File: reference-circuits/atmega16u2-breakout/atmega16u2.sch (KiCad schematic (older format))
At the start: 24 parts, among them J1 USB-MICROB, J2 ICSP, U1 IC-MCU-ATMEGA16U2-MU-VQFN32, X1 16MHz 18pF

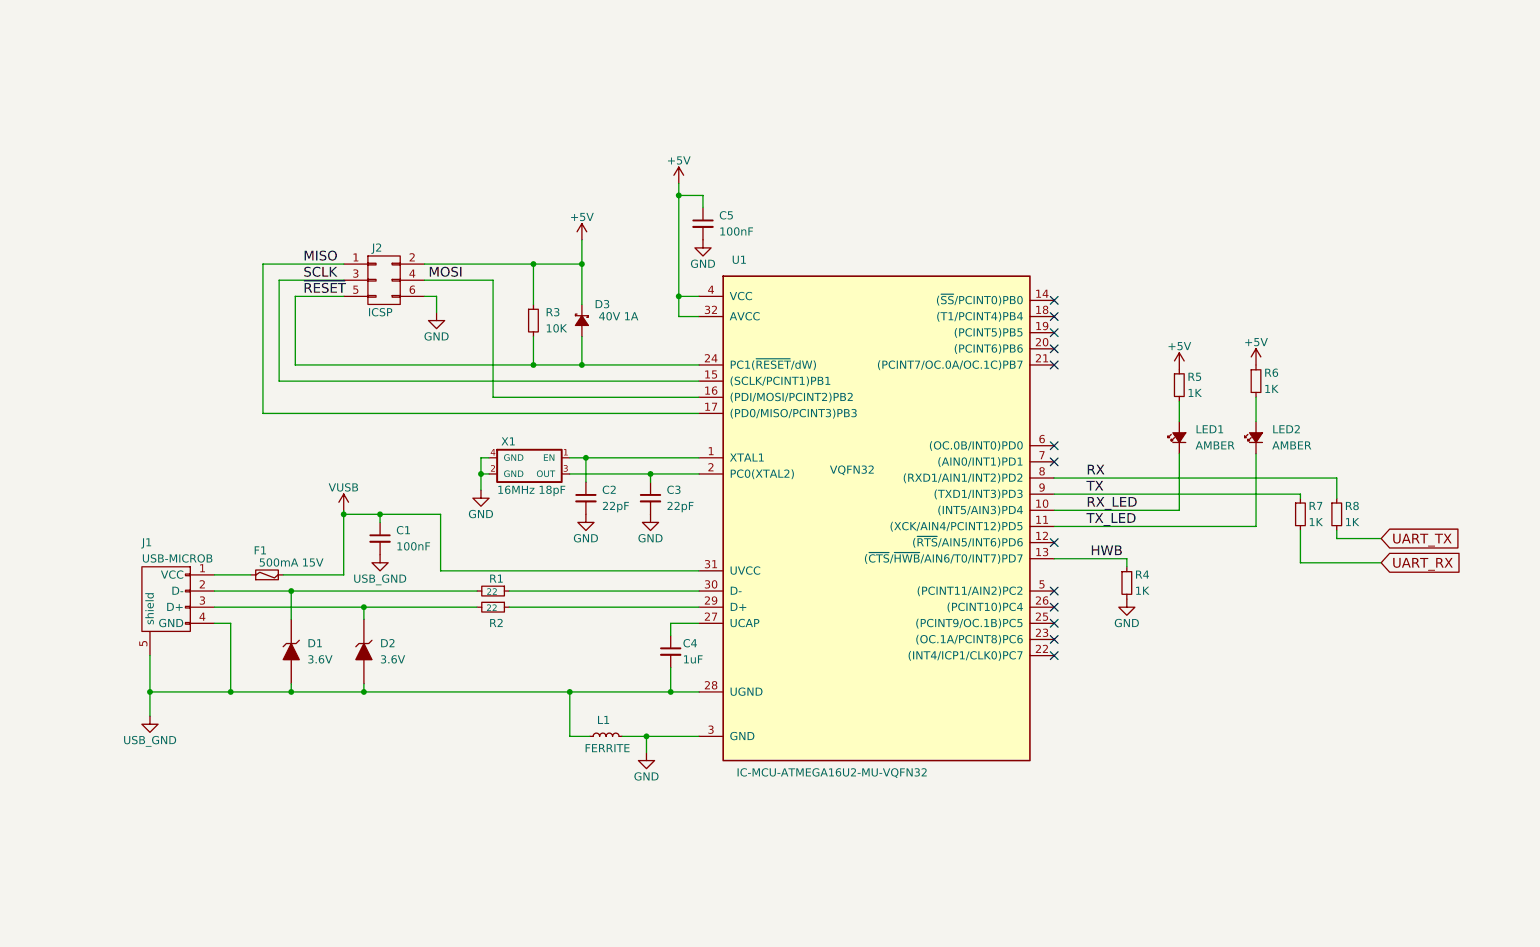
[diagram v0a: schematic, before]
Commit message: Schematic verified, printed.
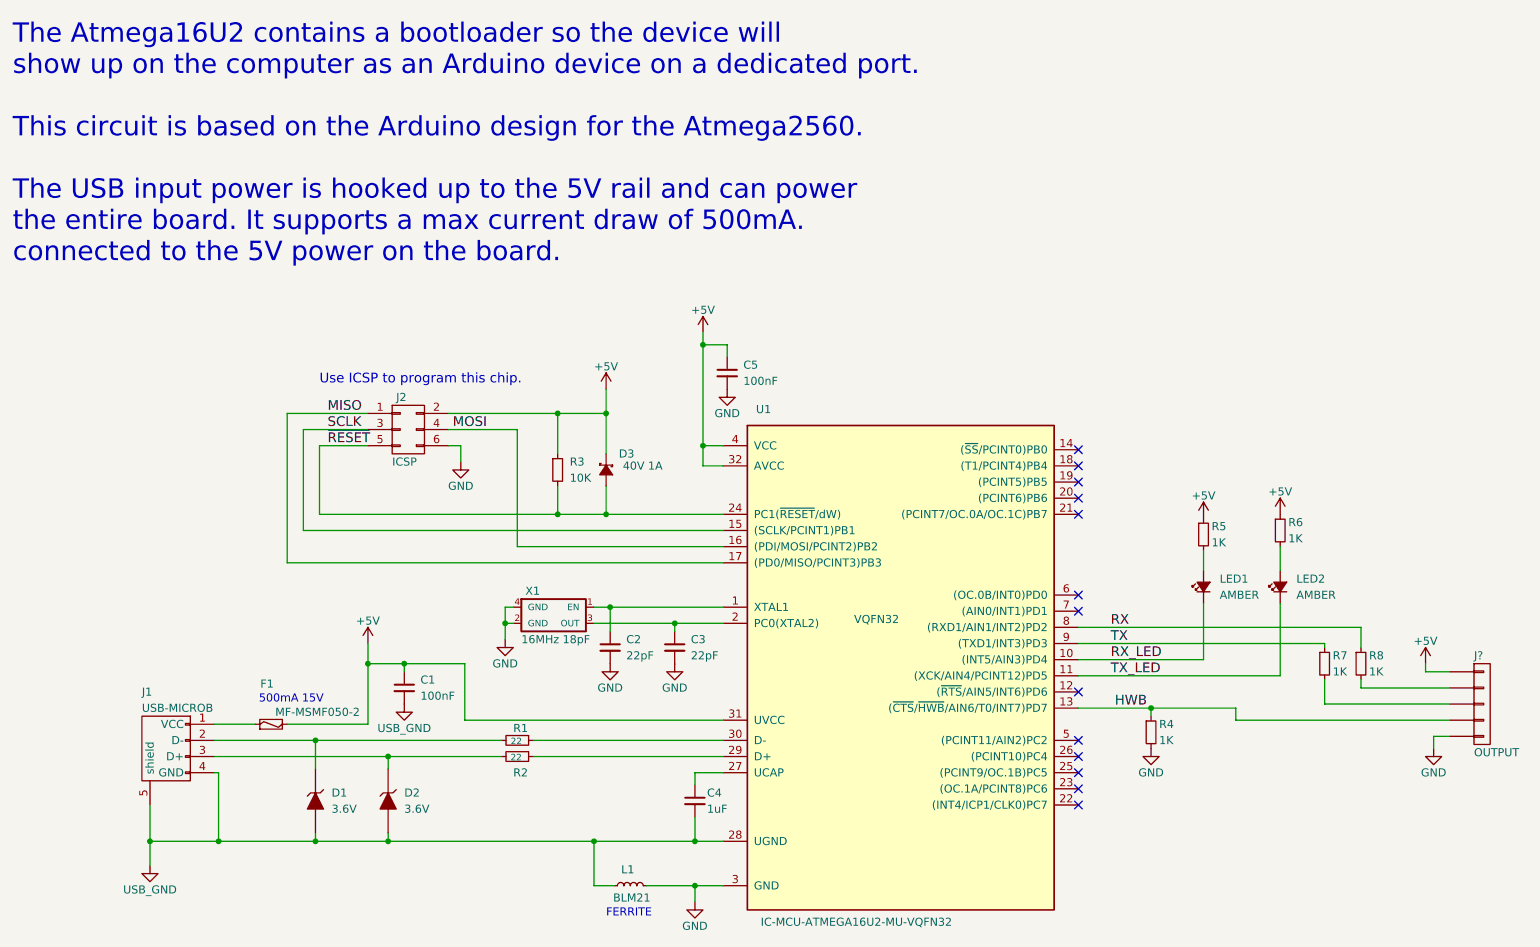
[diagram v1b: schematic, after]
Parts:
- removed J2: ICSP, CONN-215079-6, symbol HEADER-FEMALE-6POS-TH-2x3-P0.1IN
- added J2: ICSP, CONN-2x03, symbol HEADER-MALE-6POS-TH-2x3-P0.1IN
- added J?: OUTPUT, CONN-1x05-2.54MM-TH, symbol HEADER-FEMALE-5POS-TH-1x05-P0.1IN
- F1: value 500mA 15V -> MF-MSMF050-2
- L1: value FERRITE -> BLM21
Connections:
- net VUSB is gone; now on net +5V: C1.1, F1.2, U1.31 (UVCC)
- net +5V: now also J2.2 (P2), J?.1 (P1)
- net GND: now also J2.6 (P6), J?.5 (P5)
- net HWB: now also J?.4 (P4)
- net MISO: now also J2.1 (P1)
- net MOSI: now also J2.4 (P4)
- net SCLK: now also J2.3 (P3)
- net ~RESET: now also J2.5 (P5)
- net UART_RX: no longer names the net of R7.2
- net UART_RX: now also J?.3 (P3)
- net UART_TX: no longer names the net of R8.2
- net UART_TX: now also J?.2 (P2)
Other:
- note added: "500mA 15V"
- note added: "FERRITE"
- note added: "The Atmega16U2 contains a bootloader so the device will \nshow up on the computer as an Arduino device on a dedicated port.\n\nThis circuit is based on the Arduino design for the Atmega2560.\n\nThe USB input power is hooked up to the 5V rail and can power\nthe entire board. It supports a max current draw of 500mA.\nconnected to the 5V power on the board."
- note added: "Use ICSP to program this chip."
- moved on the sheet: C1, C2, C3, C4, C5, D1, D2, D3, F1, J1, L1, LED1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

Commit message: Schematic PDF created. Exported rough BOM.
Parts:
- C1, L1: footprint 0402 -> Wickerlib:0402
- C2, C3, C4, LED1, LED2, R1, R2, R4, R5, R6, R7, R8: footprint 0603 -> Wickerlib:0603
- C5, R3: footprint 0805 -> Wickerlib:0805
- D1, D2: footprint DO41 -> Wickerlib:Diode_DO-41
- D3: footprint SMA -> Wickerlib:SMA_Standard
- F1: footprint 1812 -> Wickerlib:1812
- J1: footprint USB-10118193 -> Wickerlib:USB-Micro-B-10118193_0001LF
- J2: footprint CONN-2x03 -> Wickerlib:Pin_Header_Straight_2x03
- J3: renamed from J?; footprint CONN-1x05-2.54MM-TH -> Wickerlib:Pin_Header_Straight_1x05
- U1: footprint VQFN32 -> Wickerlib:QFN-32-1EP_5x5mm_Pitch0.5mm; Package VQFN32 -> QFN32
- X1: footprint CTS-4SMD -> Wickerlib:CRYSTAL-CTS-4SMD
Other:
- moved on the sheet: J3, R8
